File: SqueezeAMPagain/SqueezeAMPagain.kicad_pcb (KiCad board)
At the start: 2 copper layers, 100 x 100 mm, 228 parts, among them J1 Conn_01x02_Pin, J10 Conn_02x07_Odd_Even, J2 Conn_01x02_Pin, J3 Conn_01x06_Pin, J4 Raspberry_Pi_2_3, J5 Conn_02x10_Odd_Even, J6 Barrel_Jack_Switch, J7 Conn_01x02_Pin, J8 USB_B_Micro, J9 Conn_01x06_Pin, Q1 Q_NPN_BEC, Q10 AO3401A, Q11 Q_NPN_BEC, Q12 AO3401A, Q13 AO3401A, Q2 AO3401A, Q3 AO3401A, Q4 AO3401A, Q5 Q_NPN_BEC, Q6 AO3401A, Q7 AO3401A, Q8 Q_NPN_BEC, Q9 Q_NPN_BEC, SW1 SW_MEC_5E, U1 TAS5756M, U2 ESP32-WROVER-E, U3 RaspberryPi_Pico_W, U4 TSOP21xx, U5 AMS1117-3.3, U6 TPS5430DDA, U7 CP2102N-Axx-xQFN28

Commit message: Update SqueezeAMPagain.kicad_pcb, SqueezeAMPagain.kicad_prl, SqueezeAMPagain.kicad_pro, and 4 more files
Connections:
- C1 pad 1: +3.3V_{SW} -> Net-(U1-CPVSS)
- C3 pad 1: +3.3V_{SW} -> Net-(U1-CPVSS)
- U1 pad 35: +3.3V_{SW} -> Net-(U1-CPVSS)
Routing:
- net +3.3V_{SW}: track 32.5 -> 14.6 mm
- net Net-(U1-CPVSS): track 0.00 -> 11.9 mm

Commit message: shrink
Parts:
- removed C56, C57, C58, C71, C91: 100n, Capacitor_SMD:C_0603_1608Metric
- removed C90: 2.2u/25V, Capacitor_SMD:C_0805_2012Metric
- removed D1: B5819W, Diode_SMD:D_SOD-123
- removed D10, D9: min. 1.4V_{ff}, LED_SMD:LED_0603_1608Metric
- removed D6, D7: LED, LED_SMD:LED_0603_1608Metric
- removed FB2: 600Ω@100MHz 500mA, Inductor_SMD:L_0805_2012Metric
- removed J4: Raspberry_Pi_2_3, Connector_PinSocket_2.54mm:PinSocket_2x20_P2.54mm_Vertical
- removed JP10, JP9: LV On, Jumper:SolderJumper-2_P1.3mm_Open_RoundedPad1.0x1.5mm
- removed JP12: P On, Jumper:SolderJumper-2_P1.3mm_Open_RoundedPad1.0x1.5mm
- removed L7: 4.7uH/4.0A, Inductor:L_Radial_D12.0mm_P5+6+7.00mm_Fastron_11P
- removed NT2: NetTie_2, NetTie:NetTie-2_SMD_Pad2.0mm
- removed Q1, Q11, Q5: Q_NPN_BEC, Package_TO_SOT_SMD:SOT-23
- removed Q10, Q12, Q2, Q6, Q7: AO3401A, Package_TO_SOT_SMD:SOT-23
- removed R15, R16, R17, R18, R19, R20, R21: 33, Resistor_SMD:R_0402_1005Metric
- removed R22, R23, R25, R28, R29, R31, R41, R42, R45, R46, R47: 10k, Resistor_SMD:R_0603_1608Metric
- removed R24, R30, R40: 150k, Resistor_SMD:R_0603_1608Metric
- removed R44: 330, Resistor_SMD:R_0603_1608Metric
- removed SW1: SW_MEC_5E, Button_Switch_SMD:SW_Push_1P1T_XKB_TS-1187A
- removed TP5: Mclk, TestPoint:TestPoint_Pad_D1.0mm
- removed U3: RaspberryPi_Pico_W, pipico_reduced:RaspberryPi_Pico_Common_THT_nokeepout
- added D11: B5819W, Diode_SMD:D_SOD-123, F.Cu at (172.3, 67.9)
- added R48: 10k, Resistor_SMD:R_0402_1005Metric, F.Cu at (171.4, 76.4)
- C12, C3, C4, C54, C6, C60, C80, C83, C84, C87, C88, C9: footprint Capacitor_SMD:C_0603_1608Metric -> Capacitor_SMD:C_0402_1005Metric
- L1, L2, L3, L4: footprint Inductor:L_Radial_D12.0mm_P5+6+7.00mm_Fastron_11P -> Inductor_SMD:L_Chilisin_BMRA00040420
- R12, R2, R3, R33, R34, R35, R36, R37, R38, R39, R4, R43, R5, R6, R7, R8: footprint Resistor_SMD:R_0603_1608Metric -> Resistor_SMD:R_0402_1005Metric
- R32: value 560R -> 10k; footprint Resistor_SMD:R_0603_1608Metric -> Resistor_SMD:R_0402_1005Metric
- moved Q8 120.9 mm to (195.2, 55.6)
- moved Q9 118.5 mm to (202.2, 56.4)
- moved C83 113.3 mm to (189.5, 23.4)
- moved C84 113.3 mm to (177.7, 34.2)
- moved C85 113.3 mm to (173.6, 37.0)
- moved C86 113.3 mm to (173.6, 34.5)
- moved C87 113.3 mm to (176.6, 36.8)
- moved C88 113.3 mm to (178.6, 36.8)
- moved C89 113.3 mm to (182.9, 37.0)
- moved D3 113.3 mm to (180.2, 32.1)
- moved FB6 113.3 mm to (175.5, 31.9)
- moved J9 113.3 mm to (186.1, 48.4)
- moved R35 113.3 mm to (173.5, 42.0)
- moved R36 113.3 mm to (173.5, 39.9)
- moved R37 113.3 mm to (173.5, 43.9)
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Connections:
- net /Pi/GPIO22 renamed /X_PSU/PON
- C11 pad 1: PVDD -> V_{IN}
- C13 pad 1: PVDD -> V_{IN}
- C14 pad 1: PVDD -> V_{IN}
- C15 pad 1: PVDD -> V_{IN}
- C16 pad 1: PVDD -> V_{IN}
- C17 pad 1: PVDD -> V_{IN}
- C18 pad 1: PVDD -> V_{IN}
- C19 pad 1: PVDD -> V_{IN}
- C2 pad 1: +3.3V_{SW} -> +3.3V
- C21 pad 1: PVDD -> V_{IN}
- C22 pad 1: PVDD -> V_{IN}
- C24 pad 1: PVDD -> V_{IN}
- C25 pad 1: PVDD -> V_{IN}
- C26 pad 1: PVDD -> V_{IN}
- C28 pad 1: PVDD -> V_{IN}
- C29 pad 1: PVDD -> V_{IN}
- C31 pad 1: PVDD -> V_{IN}
- C32 pad 1: PVDD -> V_{IN}
- C33 pad 1: PVDD -> V_{IN}
- C35 pad 1: PVDD -> V_{IN}
- C36 pad 1: PVDD -> V_{IN}
- C4 pad 1: +3.3V_{SW} -> +3.3V
- C66 pad 2: /Power/GND_{IN} -> PGND
- C68 pad 2: /Power/GND_{IN} -> PGND
- C74 pad 1: PVDD -> V_{IN}
- C76 pad 1: PVDD -> V_{IN}
- C92 pad 1: PVDD -> V_{IN}
- C93 pad 1: PVDD -> V_{IN}
- NT1 pad 2: /Power/GND_{IN} -> PGND
- R1 pad 2: /Amp/MCLK -> unconnected-(R1-Pad2)
- R13 pad 2: /Amp/MCLK -> /esp/GPIO0/BOOT/I2S0_MCLK
- R32 pad 1: Net-(C71-Pad2) -> +3.3V
- R32 pad 2: GND -> Net-(U2-GPIO0/BOOT/ADC2_CH1)
- R9 pad 1: /Pi/GPIO23 -> /esp/IO15
- TP3 pad 1: PVDD -> V_{IN}
- U1 pad 31: +3.3V_{SW} -> +3.3V
- U1 pad 41: PVDD -> V_{IN}
- U1 pad 42: PVDD -> V_{IN}
- U1 pad 43: PVDD -> V_{IN}
- U1 pad 6: PVDD -> V_{IN}
- U1 pad 7: PVDD -> V_{IN}
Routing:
- net GND: track 345.5 -> 17.5 mm, vias 40 -> 6
- net /SDA: track 222.5 -> 9.60 mm, vias 6 -> 0
- net /SCL: track 208.2 -> 0.00 mm, vias 5 -> 0
- net +3.3V: track 248.6 -> 41.4 mm, vias 5 -> 0
- net V_{USB}: track 217.8 -> 19.9 mm, vias 4 -> 0
- net /X_PSU/PON: track 161.3 -> 0.00 mm, vias 4 -> 0
- net /esp/TCK: track 130.9 -> 0.00 mm, vias 3 -> 0
- net PGND: track 155.5 -> 31.8 mm, vias 112 -> 0
- net +5V: track 139.2 -> 19.9 mm, vias 1 -> 0
- net /FPConnector/IO1: track 114.8 -> 0.00 mm, vias 2 -> 0
- net /Pi/GPIO23: track 108.9 -> 0.00 mm, vias 2 -> 0
- net /esp/TDI: track 108.8 -> 0.00 mm, vias 4 -> 0
- net /FPConnector/IO4: track 102.1 -> 0.00 mm, vias 2 -> 0
- net /USB-Uart/EN/~{RESET}: track 100.9 -> 0.00 mm, vias 2 -> 0
- net /USB-Uart/RX: track 106.5 -> 11.8 mm
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- removed copper zone on B.Cu, net /Amp/SPK_A+
- removed copper zone on F.Cu, net /Amp/SPK_A+
- removed copper zone on B.Cu, net /Amp/SPK_A-
- removed copper zone on F.Cu, net /Amp/SPK_A-
- removed copper zone on B.Cu, net /Amp/SPK_B+
- removed copper zone on F.Cu, net /Amp/SPK_B+
- removed copper zone on B.Cu, net /Amp/SPK_B-
- removed copper zone on F.Cu, net /Amp/SPK_B-
- removed copper zone on F.Cu, net /Amp/SpeakerChannelA+/Amp_out
- removed copper zone on F.Cu, net /Amp/SpeakerChannelA-/Amp_out
- removed copper zone on F.Cu, net /Amp/SpeakerChannelB+/Amp_out
- removed copper zone on F.Cu, net /Amp/SpeakerChannelB-/Amp_out
- removed copper zone on B.Cu, net /Power/GND_{IN}
- removed copper zone on F.Cu, net /Power/GND_{IN}
- removed copper zone on B.Cu, net /Power/GND_{supply}
- removed copper zone on F.Cu, net /Power/GND_{supply}
- removed copper zone on F.Cu, net /Power/V_{IN,SW}
- removed copper zone on B.Cu, net /Power/V_{supply,plug}
- removed copper zone on F.Cu, net /Power/V_{supply,plug}
- removed copper zone on B.Cu, net PGND
- removed copper zone on B.Cu, net PVDD
- removed copper zone on F.Cu, net PVDD
- removed copper zone on B.Cu, net V_{IN}
- removed copper zone on F.Cu, net V_{IN}
- removed copper zone on F.Cu, net V_{supply}

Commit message: v2
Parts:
- removed C26: 100n, Capacitor_SMD:C_0603_1608Metric
- removed the C31 at (72.0, 75.4)
- removed C32: 10u/50V, Capacitor_SMD:C_1206_3216Metric
- removed the C36 at (67.1, 76.9)
- removed the C74 at (103.9, 78.0)
- removed D8: min. 1.4V_{ff}, LED_SMD:LED_0603_1608Metric
- removed J10: Conn_02x07_Odd_Even, Connector_IDC:IDC-Header_2x07_P2.54mm_Vertical
- removed J9: Conn_01x06_Pin, Connector_PinHeader_2.54mm:PinHeader_1x06_P2.54mm_Vertical
- removed the L5 at (115.3, 70.4)
- removed the R1 at (105.6, 90.7)
- removed the TP2 at (119.6, 104.7)
- added C88: 2.2u/25V, Capacitor_SMD:C_0805_2012Metric, F.Cu at (143.1, 56.7)
- added D3: B5819W, Diode_SMD:D_SOD-123, F.Cu at (122.3, 71.4)
- added D7: 5V, Diode_SMD:D_SOD-123, F.Cu at (122.5, 56.4)
- added FB6: 600Ω@100MHz 500mA, Inductor_SMD:L_0805_2012Metric, F.Cu at (120.2, 94.0)
- added FB7: 600Ω@100MHz 500mA, Inductor_SMD:L_0805_2012Metric, F.Cu at (104.1, 87.2)
- added FB8: 600Ω@100MHz 500mA, Inductor_SMD:L_0805_2012Metric, F.Cu at (96.8, 84.0)
- added FB9: 600Ω@100MHz 500mA, Inductor_SMD:L_0805_2012Metric, F.Cu at (90.8, 84.0)
- added JP13: SolderJumper_2_Open, Jumper:SolderJumper-2_P1.3mm_Open_RoundedPad1.0x1.5mm, F.Cu at (121.8, 73.9)
- added L1: 4.7uH/6.0A, Inductor_SMD:L_Chilisin_BMRA00040420, F.Cu at (117.0, 69.3)
- added L12: 4.7uH/6.0A, Inductor_THT:L_Radial_D8.7mm_P5.00mm_Fastron_07HCP, F.Cu at (94.4, 66.8)
- added L3: 4.7uH/6.0A, Inductor_THT:L_Radial_D8.7mm_P5.00mm_Fastron_07HCP, F.Cu at (72.5, 60.2)
- added L4: 4.7uH/6.0A, Inductor_THT:L_Radial_D8.7mm_P5.00mm_Fastron_07HCP, F.Cu at (113.2, 66.2)
- added L6: 4.7uH/6.0A, Inductor_THT:L_Radial_D8.7mm_P5.00mm_Fastron_07HCP, F.Cu at (70.2, 66.2)
- added L9: 4.7uH/6.0A, Inductor_THT:L_Radial_D8.7mm_P5.00mm_Fastron_07HCP, F.Cu at (93.0, 60.0)
- added R26: 10R, Resistor_SMD:R_1206_3216Metric_Pad1.30x1.75mm_HandSolder, F.Cu at (120.9, 76.5)
- added R27: 10k, Resistor_SMD:R_0402_1005Metric, F.Cu at (66.3, 94.4)
- added SW2: SW_MEC_5G, Button_Switch_SMD:SW_Push_1P1T_XKB_TS-1187A, F.Cu at (71.4, 92.5)
- C11, C13, C14, C15, C16, C19: footprint Capacitor_THT:CP_Radial_D10.0mm_P5.00mm_P7.50mm -> Capacitor_THT:CP_Radial_D8.0mm_P3.50mm
- C24: value 100n -> 10u/50V; footprint Capacitor_SMD:C_0603_1608Metric -> Capacitor_SMD:C_1206_3216Metric
- C60: renamed from C64; footprint Capacitor_SMD:C_0603_1608Metric -> Capacitor_SMD:C_0402_1005Metric
- C73: footprint Capacitor_SMD:C_0603_1608Metric -> Capacitor_SMD:C_0402_1005Metric
- J3: value Conn_01x06_Pin -> Conn_ARM_JTAG_SWD_10; footprint Connector_PinHeader_2.54mm:PinHeader_1x06_P2.54mm_Vertical -> Connector_PinHeader_1.27mm:PinHeader_2x05_P1.27mm_Vertical_SMD
- J5: renamed from J6; footprint Connector_BarrelJack:BarrelJack_CUI_PJ-102AH_Horizontal -> Connector_BarrelJack:BarrelJack_GCT_DCJ200-10-A_Horizontal
- L14: renamed from L6; footprint Inductor_SMD:L_Chilisin_BMRB00060612 -> Inductor_SMD:L_Changjiang_FNR5020S
- R17: renamed from R27; footprint Resistor_SMD:R_0603_1608Metric -> Resistor_SMD:R_0402_1005Metric
- R18: renamed from R43; value 330 -> 1k
- R5, R7: footprint Resistor_SMD:R_0402_1005Metric -> Resistor_SMD:R_0603_1608Metric
- moved R12 91.7 mm to (151.2, 80.8), turned to 180 degrees
- moved U3 82.0 mm to (77.8, 93.3)
- moved J3 80.9 mm to (120.1, 81.5)
- moved R25 75.4 mm to (151.8, 86.0)
- moved C63 74.1 mm to (103.2, 73.3), turned to -90 degrees
- moved C69 70.1 mm to (95.4, 73.3), turned to -90 degrees
- moved C81 70.0 mm to (125.6, 52.0), turned to 180 degrees
- moved C16 69.7 mm to (108.5, 75.0), turned to -90 degrees
- moved R24 68.7 mm to (154.2, 82.8)
- moved C60 68.7 mm to (155.1, 67.6), turned to 0 degrees
- moved C62 67.2 mm to (155.2, 61.4), turned to 0 degrees
- moved C57 65.7 mm to (151.1, 88.0), turned to 180 degrees
- moved C56 62.9 mm to (150.0, 93.3)
- moved C66 62.4 mm to (114.5, 77.5), turned to -90 degrees
- moved R14 59.2 mm to (156.5, 82.5)
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- renumbered C92 to C27, C27 to C28, C28 to C30, C30 to C31, C33 to C34, C34 to C36, C37 to C38, C93 to C39, C38 to C40, C39 to C41, C40 to C42, C41 to C43, C42 to C44, C43 to C45, C44 to C46, C45 to C47, C46 to C48, C47 to C49, C48 to C50, C49 to C51, C50 to C52, C51 to C53, C52 to C54, C53 to C55, C54 to C56, C55 to C57, C59 to C58, C60 to C59, C66 to C63, C63 to C64, C68 to C66, C76 to C69, C69 to C70, C70 to C71, C75 to C74, C77 to C75, C78 to C76, C79 to C77, C80 to C78, C81 to C79, C82 to C80, C83 to C81, C84 to C82, C85 to C83, C86 to C84, C87 to C85, C88 to C86, C89 to C87, D4 to D1, D11 to D2, D5 to D4, D2 to D5, D3 to D6, FB3 to FB2, FB4 to FB3, FB5 to FB4, FB6 to FB5, J5 to J4, J7 to J6, J8 to J7, JP11 to JP10, JP13 to JP11, JP14 to JP9, L4 to L11, L1 to L2, L2 to L5, L3 to L8, Q13 to Q1, Q3 to Q2, Q4 to Q3, Q8 to Q4, Q9 to Q5, R48 to R1, R32 to R13, R13 to R14, R14 to R15, R26 to R16, R33 to R19, R34 to R20, R35 to R21, R36 to R22, R37 to R23, R38 to R24, R39 to R25, TP6 to TP1, TP11 to TP10, TP12 to TP11, TP7 to TP2, TP8 to TP3, TP9 to TP4, TP10 to TP5, TP1 to TP6, TP3 to TP8, TP4 to TP9, U4 to U3, U5 to U4, U6 to U5, U7 to U6
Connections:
- net +3.3V_{SW} renamed Net-(U1-DVDD)
- C11 pad 1: V_{IN} -> PVDD
- C13 pad 1: V_{IN} -> PVDD
- C14 pad 1: V_{IN} -> PVDD
- C15 pad 1: V_{IN} -> PVDD
- C16 pad 1: V_{IN} -> PVDD
- C17 pad 1: V_{IN} -> PVDD
- C18 pad 1: V_{IN} -> PVDD
- C19 pad 1: V_{IN} -> PVDD
- C2 pad 1: +3.3V -> Net-(U1-CPVDD)
- C21 pad 1: V_{IN} -> PVDD
- C22 pad 1: V_{IN} -> PVDD
- C24 pad 1: V_{IN} -> PVDD
- C25 pad 1: V_{IN} -> PVDD
- C27 pad 1: V_{IN} -> PVDD
- C29 pad 1: V_{IN} -> PVDD
- C30 pad 1: V_{IN} -> PVDD
- C34 pad 1: V_{IN} -> PVDD
- C35 pad 1: V_{IN} -> PVDD
- C39 pad 1: V_{IN} -> PVDD
- C4 pad 1: +3.3V -> Net-(U1-CPVDD)
- C63 pad 1: V_{IN} -> PVDD
- C66 pad 1: V_{IN} -> PVDD
- C69 pad 1: V_{IN} -> PVDD
- D2 pad 2: V_{IN} -> V_{supply}
- J3 pad 1: /esp/TDO -> +3.3V
- J3 pad 2: /esp/TCK -> /esp/TMS
- J3 pad 3: /esp/TDI -> GND
- J3 pad 4: /esp/TMS -> /esp/TCK
- J3 pad 5: +3.3V -> GND
- J3 pad 6: GND -> /esp/TDO
- J4 pad 1: unconnected-(J5-Pin_1-Pad1) -> GND
- J4 pad 10: +3.3V -> /FPConnector/IO1
- J4 pad 2: unconnected-(J5-Pin_2-Pad2) -> Net-(J4-Pin_2)
- J4 pad 3: GND -> /esp/TCK
- J4 pad 6: /FPConnector/IO3 -> /FPConnector/IO6
- J4 pad 8: /FPConnector/IO1 -> /FPConnector/IO3
- J4 pad 9: +3.3V -> Net-(J4-Pin_9)
- R14 pad 2: /esp/GPIO0/BOOT/I2S0_MCLK -> /USB-Uart/BOOT
- R9 pad 1: /esp/IO15 -> /FPConnector/~{WAKE}
- TP8 pad 1: V_{IN} -> PVDD
- U1 pad 31: +3.3V -> Net-(U1-CPVDD)
- U1 pad 41: V_{IN} -> PVDD
- U1 pad 42: V_{IN} -> PVDD
- U1 pad 43: V_{IN} -> PVDD
- U1 pad 6: V_{IN} -> PVDD
- U1 pad 7: V_{IN} -> PVDD
- U2 pad 12: /X_PSU/PON -> /FPConnector/IO6
- U3 pad 2: +3.3V -> Net-(J4-Pin_9)
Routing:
- net GND: track 17.5 -> 199.5 mm, vias 6 -> 31
- net +3.3V: track 41.4 -> 196.3 mm, vias 0 -> 20
- net /Amp/~{SPK_FAULT}: track 0.00 -> 84.1 mm, vias 0 -> 2
- net /esp/TMS: track 0.00 -> 80.7 mm, vias 0 -> 3
- net /SCL: track 0.00 -> 74.0 mm, vias 0 -> 1
- net /FPConnector/IO4: track 0.00 -> 68.3 mm, vias 0 -> 2
- net /SDA: track 9.60 -> 75.4 mm, vias 0 -> 1
- net /FPConnector/D/C: track 0.00 -> 65.8 mm, vias 0 -> 1
- net /FPConnector/~{WAKE}: track 0.00 -> 65.3 mm
- net /esp/TDI: track 0.00 -> 61.6 mm, vias 0 -> 2
- net /FPConnector/IO1: track 0.00 -> 53.5 mm, vias 0 -> 2
- net /FPConnector/IO2: track 0.00 -> 52.7 mm, vias 0 -> 1
- net /FPConnector/IO3: track 0.00 -> 52.6 mm, vias 0 -> 1
- net /FPConnector/IO6: track 0.00 -> 52.1 mm, vias 0 -> 2
- net /Amp/SCLK: track 0.00 -> 49.4 mm, vias 0 -> 2
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- added copper zone on B.Cu, net +3.3V
- added copper zone on B.Cu, net /Amp/SPK_A+
- added copper zone on F.Cu, net /Amp/SPK_A+
- added copper zone on B.Cu, net /Amp/SPK_A-
- added copper zone on F.Cu, net /Amp/SPK_A-
- added copper zone on B.Cu, net /Amp/SPK_B+
- added copper zone on F.Cu, net /Amp/SPK_B+
- added copper zone on B.Cu, net /Amp/SPK_B-
- added copper zone on F.Cu, net /Amp/SPK_B-
- added copper zone on F.Cu, net /Amp/SpeakerChannelA+/Amp_out
- added copper zone on F.Cu, net /Amp/SpeakerChannelA-/Amp_out
- added copper zone on F.Cu, net /Amp/SpeakerChannelB+/Amp_out
- added copper zone on F.Cu, net /Amp/SpeakerChannelB-/Amp_out
- added copper zone on B.Cu, net /Power/GND_{supply}
- added copper zone on F.Cu, net /Power/GND_{supply}
- added copper zone on B.Cu, net /Power/V_{supply,plug}
- added copper zone on F.Cu, net /Power/V_{supply,plug}
- added copper zone on B.Cu, net PGND
- added copper zone on B.Cu, net PVDD
- added copper zone on F.Cu, net PVDD
- added copper zone on B.Cu, net V_{supply}
- added copper zone on F.Cu, net V_{supply}
- removed copper zone on F.Cu, net Net-(U1-DVDD)
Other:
- board size 100 x 100 mm -> 100 x 50 mm
- board text added: "2"
- board text added: "v"
- board text removed: "3V3 On"
- board text removed: "E"
- board text removed: "LV ON"
- board text removed: "MCLK"
- board text removed: "P"
- board text removed: "P ON"
- board text removed: "PVDD On"
- board text removed: "R"
- board text removed: "V_{IN}"
- board text removed: "V_{supply}"

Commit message: wip
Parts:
- moved C47 4.06 mm to (67.5, 60.2)
- moved C46 3.10 mm to (68.0, 56.5)
- moved FB7 2.78 mm to (106.5, 85.8)
- moved R3 1.49 mm to (122.6, 92.4), turned to 0 degrees
- moved R2 1.40 mm to (122.6, 93.8), turned to -90 degrees
- moved R9 1.00 mm to (120.2, 91.0)
- moved TP4 0.82 mm to (124.6, 91.8)
- moved D7 0.82 mm to (122.0, 57.0)
- moved R4 0.72 mm to (63.4, 86.4)
- moved R5 0.63 mm to (63.4, 83.8)
- moved L11 0.60 mm to (97.2, 66.1)
- moved L12 0.52 mm to (94.8, 66.4), turned to 5 degrees
- moved R16 0.50 mm to (120.0, 56.2)
- moved R7 0.40 mm to (63.4, 80.7)
- moved TP2 0.35 mm to (112.6, 81.5)
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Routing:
- net /FPConnector/IO3: track 52.6 -> 44.2 mm
- net /SCL: track 74.0 -> 80.3 mm
- net /FPConnector/~{WAKE}: track 65.3 -> 60.1 mm
- net Net-(J4-Pin_9): track 28.7 -> 31.7 mm
- net Net-(U2-GPIO0/BOOT/ADC2_CH1): track 35.2 -> 32.6 mm
- net /Amp/~{SPK_FAULT}: track 84.1 -> 86.5 mm
- net /SDA: track 75.4 -> 72.9 mm
- net GND: track 199.5 -> 197.3 mm
- net +3.3V: track 196.3 -> 198.2 mm
- net /FPConnector/IO2: track 52.7 -> 54.6 mm
- net Net-(U2-32K_XP/GPIO32/ADC1_CH4): track 36.9 -> 38.6 mm
- net /FPConnector/IO1: track 53.5 -> 55.2 mm
- net /USB-Uart/EN/~{RESET}: track 45.4 -> 47.0 mm
- net /esp/TDI: track 61.6 -> 63.0 mm
- net Net-(JP1-B): track 35.1 -> 36.3 mm
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
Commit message: wip
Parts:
- removed C65: 2.2u/25V, Capacitor_SMD:C_0805_2012Metric
- added FB10: 600Ω@100MHz 500mA, Inductor_SMD:L_0805_2012Metric, F.Cu at (120.3, 93.2)
- moved R14 31.8 mm to (126.0, 91.6), turned to -90 degrees
- moved R13 31.4 mm to (124.0, 91.6), turned to 90 degrees
- moved Q5 28.5 mm to (128.4, 93.0), turned to 180 degrees
- moved C56 27.5 mm to (149.3, 65.8), turned to 0 degrees
- moved R1 27.1 mm to (124.0, 74.6)
- moved TP10 26.8 mm to (142.4, 92.2)
- moved R24 25.4 mm to (131.5, 94.0), turned to 180 degrees
- moved R2 25.1 mm to (147.6, 92.2), turned to 90 degrees
- moved TP4 24.6 mm to (149.2, 92.2)
- moved R3 24.0 mm to (146.6, 92.2), turned to 90 degrees
- moved C57 23.8 mm to (156.2, 64.8), turned to -90 degrees
- moved R25 21.1 mm to (131.5, 92.0), turned to 0 degrees
- moved TP5 20.6 mm to (145.0, 92.2)
- moved Q4 19.2 mm to (134.6, 93.0), turned to 0 degrees
- moved TP6 18.2 mm to (139.4, 92.2)
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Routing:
- net +5V: track 26.4 -> 88.2 mm, vias 0 -> 4
- net /FPConnector/IO3: track 44.2 -> 74.9 mm
- net /FPConnector/MOSI: track 38.7 -> 63.0 mm
- net /USB-Uart/EN/~{RESET}: track 47.0 -> 70.8 mm, vias 2 -> 4
- net /SCL: track 80.3 -> 102.9 mm
- net /SDA: track 72.9 -> 94.1 mm
- net Net-(U2-GPIO0/BOOT/ADC2_CH1): track 32.6 -> 16.7 mm
- net Net-(Q4-E): track 41.7 -> 54.2 mm
- net /FPConnector/SCK: track 42.4 -> 55.0 mm
- net /FPConnector/MISO: track 39.7 -> 51.6 mm
- net /FPConnector/D/C: track 66.7 -> 55.1 mm
- net Net-(U5-VIN): track 43.6 -> 32.0 mm, vias 3 -> 2
- net /esp/TMS: track 81.8 -> 70.7 mm
- net Net-(U2-DAC_1/ADC2_CH8/GPIO25): track 43.1 -> 32.2 mm, vias 2 -> 0
- net Net-(Q5-E): track 47.2 -> 57.9 mm
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- removed copper zone on B.Cu, net +3.3V

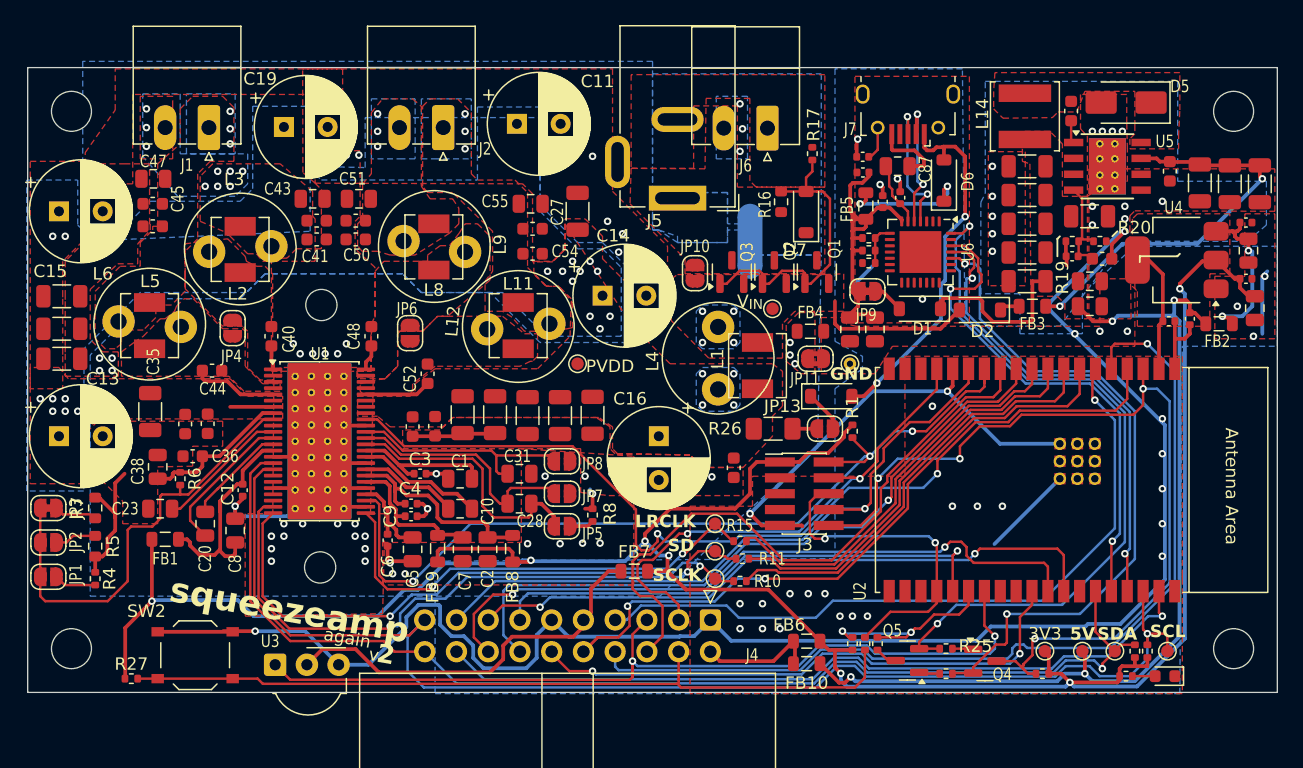
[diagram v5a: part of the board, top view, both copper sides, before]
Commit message: round edges
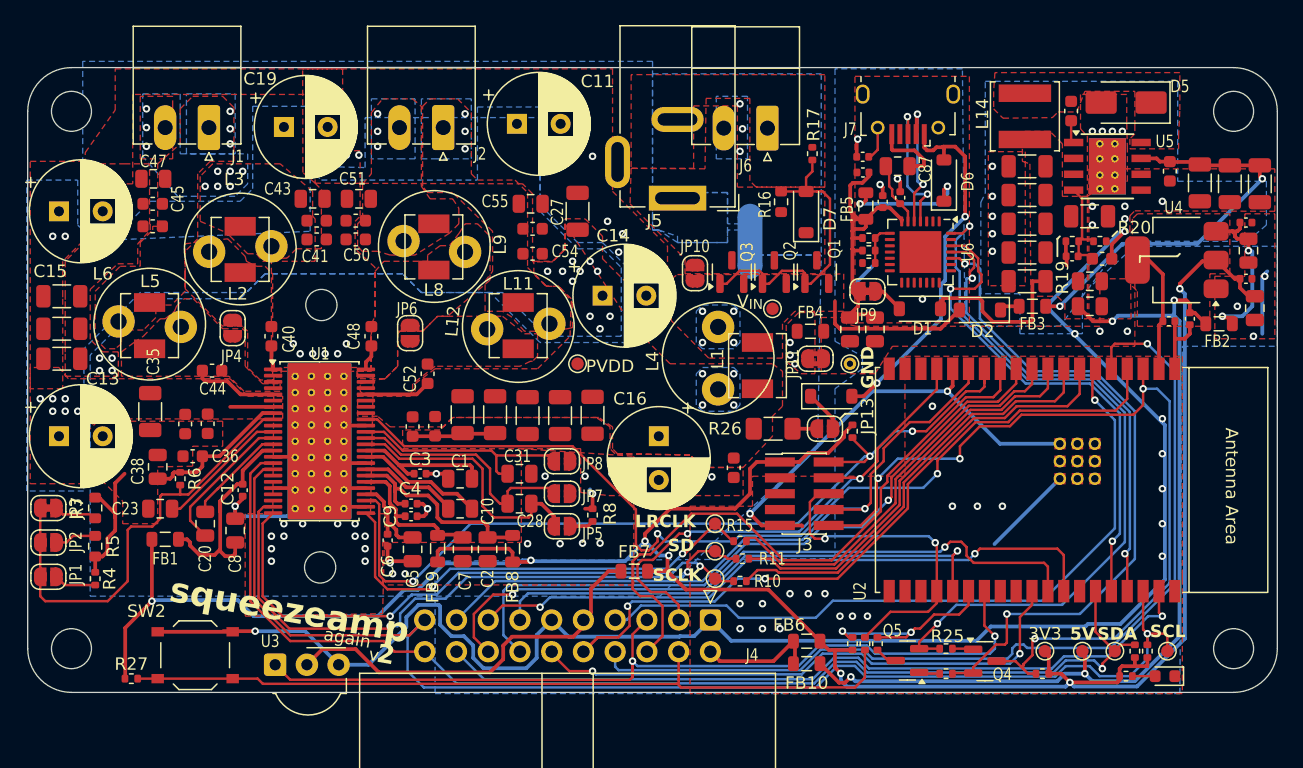
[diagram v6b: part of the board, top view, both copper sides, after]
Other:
- outline, holes or cut-outs redrawn
- board text removed: "V_{USB}"
